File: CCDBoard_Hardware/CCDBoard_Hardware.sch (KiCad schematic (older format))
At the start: 3 parts

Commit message: Associated footprints and generated netlist
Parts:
- Conn1: renamed from Conn?; value Molex_SL_02 -> Molex_SL_04; footprint (none) -> MRDT_Connectors:MOLEX_SL_04_Horizontal
- Conn2: renamed from Conn?; footprint (none) -> MRDT_Connectors:MOLEX_SL_07_Horizontal
- U1: renamed from U?; footprint (none) -> MRDT_Sensors:TCD-1304
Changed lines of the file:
@@
 EESchema Schematic File Version 4
+LIBS:CCDBoard_Hardware-cache
 EELAYER 26 0
 EELAYER END
@@
 $EndDescr
 $Comp
-L MRDT_Sensors:TCD1304 U?
+L MRDT_Sensors:TCD1304 U1
 U 1 1 5C83DD52
 P 4500 2600
-F 0 "U?" H 4700 3175 50  0000 C CNN
+F 0 "U1" H 4700 3175 50  0000 C CNN
 F 1 "TCD1304" H 4700 3084 50  0000 C CNN
-F 2 "" H 4200 2100 50  0001 C CNN
+F 2 "MRDT_Sensors:TCD-1304" H 4200 2100 50  0001 C CNN
 F 3 "" H 4200 2100 50  0001 C CNN
 	1    4500 2600
@@
 $EndComp
 $Comp
-L power:GND #PWR?
+L power:GND #PWR0101
 U 1 1 5C83DDBD
 P 4350 2550
-F 0 "#PWR?" H 4350 2300 50  0001 C CNN
+F 0 "#PWR0101" H 4350 2300 50  0001 C CNN
 F 1 "GND" H 4355 2377 50  0000 C CNN
 F 2 "" H 4350 2550 50  0001 C CNN
@@
 $EndComp
 $Comp
-L power:+3V3 #PWR?
+L power:+3V3 #PWR0102
 U 1 1 5C83DE2E
 P 4350 2250
-F 0 "#PWR?" H 4350 2100 50  0001 C CNN
+F 0 "#PWR0102" H 4350 2100 50  0001 C CNN
 F 1 "+3V3" H 4365 2423 50  0000 C CNN
 F 2 "" H 4350 2250 50  0001 C CNN
@@
 	5050 2550 5000 2550
 $Comp
-L MRDT_Connectors:Molex_SL_07 Conn?
+L MRDT_Connectors:Molex_SL_07 Conn2
 U 1 1 5C83E06D
 P 6050 3800
-F 0 "Conn?" H 6050 3750 60  0000 L CNN
+F 0 "Conn2" H 6050 3750 60  0000 L CNN
 F 1 "Molex_SL_07" H 6177 4102 60  0000 L CNN
-F 2 "" H 6050 4000 60  0001 C CNN
+F 2 "MRDT_Connectors:MOLEX_SL_07_Horizontal" H 6050 4000 60  0001 C CNN
 F 3 "" H 6050 4000 60  0001 C CNN
 	1    6050 3800
@@
 $EndComp
 $Comp
-L power:+3V3 #PWR?
+L power:+3V3 #PWR0103
 U 1 1 5C83E099
 P 5800 3100
-F 0 "#PWR?" H 5800 2950 50  0001 C CNN
+F 0 "#PWR0103" H 5800 2950 50  0001 C CNN
 F 1 "+3V3" H 5815 3273 50  0000 C CNN
 F 2 "" H 5800 3100 50  0001 C CNN
@@
 $EndComp
 $Comp
-L power:GND #PWR?
+L power:GND #PWR0104
 U 1 1 5C83E0A8
 P 5800 3800
-F 0 "#PWR?" H 5800 3550 50  0001 C CNN
+F 0 "#PWR0104" H 5800 3550 50  0001 C CNN
 F 1 "GND" H 5805 3627 50  0000 C CNN
 F 2 "" H 5800 3800 50  0001 C CNN
@@
 $EndComp
 $Comp
-L MRDT_Connectors:Molex_SL_04 Conn?
+L MRDT_Connectors:Molex_SL_04 Conn1
 U 1 1 5C83E20B
 P 6050 2600
-F 0 "Conn?" H 6050 2550 60  0000 L CNN
-F 1 "Molex_SL_02" H 6177 2752 60  0000 L CNN
-F 2 "" H 6050 2500 60  0001 C CNN
+F 0 "Conn1" H 6050 2550 60  0000 L CNN
+F 1 "Molex_SL_04" H 6177 2752 60  0000 L CNN
+F 2 "MRDT_Connectors:MOLEX_SL_04_Horizontal" H 6050 2500 60  0001 C CNN
 F 3 "" H 6050 2500 60  0001 C CNN
 	1    6050 2600
@@
 $EndComp
 $Comp
-L power:GND #PWR?
+L power:GND #PWR0105
 U 1 1 5C83E23F
 P 5800 2600
-F 0 "#PWR?" H 5800 2350 50  0001 C CNN
+F 0 "#PWR0105" H 5800 2350 50  0001 C CNN
 F 1 "GND" H 5805 2427 50  0000 C CNN
 F 2 "" H 5800 2600 50  0001 C CNN

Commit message: updates Sensorboard connector
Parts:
- Conn1: value Molex_SL_04 -> Molex_SL_05; footprint MRDT_Connectors:MOLEX_SL_04_Horizontal -> MRDT_Connectors:MOLEX_SL_05_Horizontal; symbol MRDT_Connectors:Molex_SL_04 -> MRDT_Connectors:Molex_SL_05
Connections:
- wire segments 24 -> 26
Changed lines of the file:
@@
 $EndComp
 $Comp
-L MRDT_Connectors:Molex_SL_04 Conn1
+L MRDT_Connectors:Molex_SL_05 Conn1
 U 1 1 5C83E20B
 P 6050 2600
 F 0 "Conn1" H 6050 2550 60  0000 L CNN
-F 1 "Molex_SL_04" H 6177 2752 60  0000 L CNN
-F 2 "MRDT_Connectors:MOLEX_SL_04_Horizontal" H 6050 2500 60  0001 C CNN
+F 1 "Molex_SL_05" H 6177 2752 60  0000 L CNN
+F 2 "MRDT_Connectors:MOLEX_SL_05_Horizontal" H 6050 2500 60  0001 C CNN
 F 3 "" H 6050 2500 60  0001 C CNN
 	1    6050 2600
@@
 Text Notes 6650 2300 2    50   ~ 0
 Reading TIVA
+$Comp
+L power:+3V3 #PWR?
+U 1 1 5C84E599
+P 5800 2100
+F 0 "#PWR?" H 5800 1950 50  0001 C CNN
+F 1 "+3V3" H 5815 2273 50  0000 C CNN
+F 2 "" H 5800 2100 50  0001 C CNN
+F 3 "" H 5800 2100 50  0001 C CNN
+	1    5800 2100
+	1    0    0    -1
+$EndComp
+Wire Wire Line
+	5850 2150 5800 2150
+Wire Wire Line
+	5800 2150 5800 2100
 $EndSCHEMATC

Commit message: Layout and step
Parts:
- Conn1: footprint MRDT_Connectors:MOLEX_SL_05_Horizontal -> MRDT_Connectors:MOLEX_SL_05_Vertical
- Conn2: footprint MRDT_Connectors:MOLEX_SL_07_Horizontal -> MRDT_Connectors:MOLEX_SL_07_Vertical
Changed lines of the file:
@@
 F 0 "Conn2" H 6050 3750 60  0000 L CNN
 F 1 "Molex_SL_07" H 6177 4102 60  0000 L CNN
-F 2 "MRDT_Connectors:MOLEX_SL_07_Horizontal" H 6050 4000 60  0001 C CNN
+F 2 "MRDT_Connectors:MOLEX_SL_07_Vertical" H 6050 4000 60  0001 C CNN
 F 3 "" H 6050 4000 60  0001 C CNN
 	1    6050 3800
@@
 F 0 "Conn1" H 6050 2550 60  0000 L CNN
 F 1 "Molex_SL_05" H 6177 2752 60  0000 L CNN
-F 2 "MRDT_Connectors:MOLEX_SL_05_Horizontal" H 6050 2500 60  0001 C CNN
+F 2 "MRDT_Connectors:MOLEX_SL_05_Vertical" H 6050 2500 60  0001 C CNN
 F 3 "" H 6050 2500 60  0001 C CNN
 	1    6050 2600
@@
 Reading TIVA
 $Comp
-L power:+3V3 #PWR?
+L power:+3V3 #PWR0106
 U 1 1 5C84E599
 P 5800 2100
-F 0 "#PWR?" H 5800 1950 50  0001 C CNN
+F 0 "#PWR0106" H 5800 1950 50  0001 C CNN
 F 1 "+3V3" H 5815 2273 50  0000 C CNN
 F 2 "" H 5800 2100 50  0001 C CNN

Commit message: Making new symbols and board for spec
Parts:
- removed Conn1: Molex_SL_05, MRDT_Connectors:MOLEX_SL_05_Vertical, symbol MRDT_Connectors:Molex_SL_05
- removed Conn2: Molex_SL_07, MRDT_Connectors:MOLEX_SL_07_Vertical, symbol MRDT_Connectors:Molex_SL_07
- removed U1: TCD1304, MRDT_Sensors:TCD-1304, symbol MRDT_Sensors:TCD1304
- added U?: S11639-01, symbol MRDT_ICs:S11639-01
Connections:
- net labels removed: +3V3, GND, ICG, M, OS, SH, Sync1, Sync2
- wire segments 26 -> 0
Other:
- note removed: "Clocking TIVA"
- note removed: "Reading TIVA"
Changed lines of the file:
@@
 EESchema Schematic File Version 4
 LIBS:CCDBoard_Hardware-cache
-EELAYER 26 0
+EELAYER 30 0
 EELAYER END
 $Descr A4 11693 8268
@@
 $EndDescr
 $Comp
-L MRDT_Sensors:TCD1304 U1
-U 1 1 5C83DD52
-P 4500 2600
-F 0 "U1" H 4700 3175 50  0000 C CNN
-F 1 "TCD1304" H 4700 3084 50  0000 C CNN
-F 2 "MRDT_Sensors:TCD-1304" H 4200 2100 50  0001 C CNN
-F 3 "" H 4200 2100 50  0001 C CNN
-	1    4500 2600
+L MRDT_ICs:S11639-01 U?
+U 1 1 5D9443A9
+P 2100 1200
+F 0 "U?" H 2100 1325 50  0000 C CNN
+F 1 "S11639-01" H 2100 1234 50  0000 C CNN
+F 2 "" H 2100 1200 50  0001 C CNN
+F 3 "" H 2100 1200 50  0001 C CNN
+	1    2100 1200
 	1    0    0    -1
 $EndComp
-$Comp
-L power:GND #PWR0101
-U 1 1 5C83DDBD
-P 4350 2550
-F 0 "#PWR0101" H 4350 2300 50  0001 C CNN
-F 1 "GND" H 4355 2377 50  0000 C CNN
-F 2 "" H 4350 2550 50  0001 C CNN
-F 3 "" H 4350 2550 50  0001 C CNN
-	1    4350 2550
-	1    0    0    -1
-$EndComp
-$Comp
-L power:+3V3 #PWR0102
-U 1 1 5C83DE2E
-P 4350 2250
-F 0 "#PWR0102" H 4350 2100 50  0001 C CNN
-F 1 "+3V3" H 4365 2423 50  0000 C CNN
-F 2 "" H 4350 2250 50  0001 C CNN
-F 3 "" H 4350 2250 50  0001 C CNN
-	1    4350 2250
-	1    0    0    -1
-$EndComp
-Wire Wire Line
-	4400 2500 4350 2500
-Wire Wire Line
-	4350 2500 4350 2550
-Wire Wire Line
-	4400 2400 4350 2400
-Wire Wire Line
-	4350 2400 4350 2300
-Wire Wire Line
-	4400 2300 4350 2300
-Connection ~ 4350 2300
-Wire Wire Line
-	4350 2300 4350 2250
-Text GLabel 5800 3650 0    50   Output ~ 0
-M
-Text GLabel 5800 3550 0    50   Output ~ 0
-SH
-Text GLabel 5800 3450 0    50   Output ~ 0
-ICG
-Text GLabel 5800 2450 0    50   Input ~ 0
-OS
-Wire Wire Line
-	5000 2250 5050 2250
-Wire Wire Line
-	5000 2350 5050 2350
-Wire Wire Line
-	5000 2450 5050 2450
-Wire Wire Line
-	5050 2550 5000 2550
-$Comp
-L MRDT_Connectors:Molex_SL_07 Conn2
-U 1 1 5C83E06D
-P 6050 3800
-F 0 "Conn2" H 6050 3750 60  0000 L CNN
-F 1 "Molex_SL_07" H 6177 4102 60  0000 L CNN
-F 2 "MRDT_Connectors:MOLEX_SL_07_Vertical" H 6050 4000 60  0001 C CNN
-F 3 "" H 6050 4000 60  0001 C CNN
-	1    6050 3800
-	1    0    0    -1
-$EndComp
-$Comp
-L power:+3V3 #PWR0103
-U 1 1 5C83E099
-P 5800 3100
-F 0 "#PWR0103" H 5800 2950 50  0001 C CNN
-F 1 "+3V3" H 5815 3273 50  0000 C CNN
-F 2 "" H 5800 3100 50  0001 C CNN
-F 3 "" H 5800 3100 50  0001 C CNN
-	1    5800 3100
-	1    0    0    -1
-$EndComp
-$Comp
-L power:GND #PWR0104
-U 1 1 5C83E0A8
-P 5800 3800
-F 0 "#PWR0104" H 5800 3550 50  0001 C CNN
-F 1 "GND" H 5805 3627 50  0000 C CNN
-F 2 "" H 5800 3800 50  0001 C CNN
-F 3 "" H 5800 3800 50  0001 C CNN
-	1    5800 3800
-	1    0    0    -1
-$EndComp
-$Comp
-L MRDT_Connectors:Molex_SL_05 Conn1
-U 1 1 5C83E20B
-P 6050 2600
-F 0 "Conn1" H 6050 2550 60  0000 L CNN
-F 1 "Molex_SL_05" H 6177 2752 60  0000 L CNN
-F 2 "MRDT_Connectors:MOLEX_SL_05_Vertical" H 6050 2500 60  0001 C CNN
-F 3 "" H 6050 2500 60  0001 C CNN
-	1    6050 2600
-	1    0    0    -1
-$EndComp
-$Comp
-L power:GND #PWR0105
-U 1 1 5C83E23F
-P 5800 2600
-F 0 "#PWR0105" H 5800 2350 50  0001 C CNN
-F 1 "GND" H 5805 2427 50  0000 C CNN
-F 2 "" H 5800 2600 50  0001 C CNN
-F 3 "" H 5800 2600 50  0001 C CNN
-	1    5800 2600
-	1    0    0    -1
-$EndComp
-Text GLabel 5050 2250 2    50   Input ~ 0
-M
-Text GLabel 5050 2350 2    50   Input ~ 0
-SH
-Text GLabel 5050 2450 2    50   Input ~ 0
-ICG
-Text GLabel 5050 2550 2    50   Output ~ 0
-OS
-Wire Wire Line
-	5850 3450 5800 3450
-Wire Wire Line
-	5850 3550 5800 3550
-Wire Wire Line
-	5850 3650 5800 3650
-Wire Wire Line
-	5850 3750 5800 3750
-Wire Wire Line
-	5800 3750 5800 3800
-Wire Wire Line
-	5850 3150 5800 3150
-Wire Wire Line
-	5800 3150 5800 3100
-Text GLabel 5800 3350 0    50   Output ~ 0
-Sync1
-Text GLabel 5800 3250 0    50   Output ~ 0
-Sync2
-Wire Wire Line
-	5850 3250 5800 3250
-Wire Wire Line
-	5850 3350 5800 3350
-Text GLabel 5800 2350 0    50   Input ~ 0
-Sync1
-Text GLabel 5800 2250 0    50   Input ~ 0
-Sync2
-Wire Wire Line
-	5850 2550 5800 2550
-Wire Wire Line
-	5800 2550 5800 2600
-Wire Wire Line
-	5850 2450 5800 2450
-Wire Wire Line
-	5850 2350 5800 2350
-Wire Wire Line
-	5850 2250 5800 2250
-Text Notes 6700 3200 2    50   ~ 0
-Clocking TIVA
-Text Notes 6650 2300 2    50   ~ 0
-Reading TIVA
-$Comp
-L power:+3V3 #PWR0106
-U 1 1 5C84E599
-P 5800 2100
-F 0 "#PWR0106" H 5800 1950 50  0001 C CNN
-F 1 "+3V3" H 5815 2273 50  0000 C CNN
-F 2 "" H 5800 2100 50  0001 C CNN
-F 3 "" H 5800 2100 50  0001 C CNN
-	1    5800 2100
-	1    0    0    -1
-$EndComp
-Wire Wire Line
-	5850 2150 5800 2150
-Wire Wire Line
-	5800 2150 5800 2100
 $EndSCHEMATC

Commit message: New shematic
this might be completly wrong. IDK
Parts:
- added C? (x6): C_Small, symbol Device:C_Small
- added C? (x4): CP_Small, symbol Device:CP_Small
- added R? (x4): R, symbol Device:R
- added U?: OPAMP, symbol pspice:OPAMP
- U?: symbol MRDT_ICs:S11639-01 -> CCDBoard_Hardware-rescue:S11639-01-MRDT_ICs
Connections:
- net labels added: +5V, 0, Video
- wire segments 0 -> 67

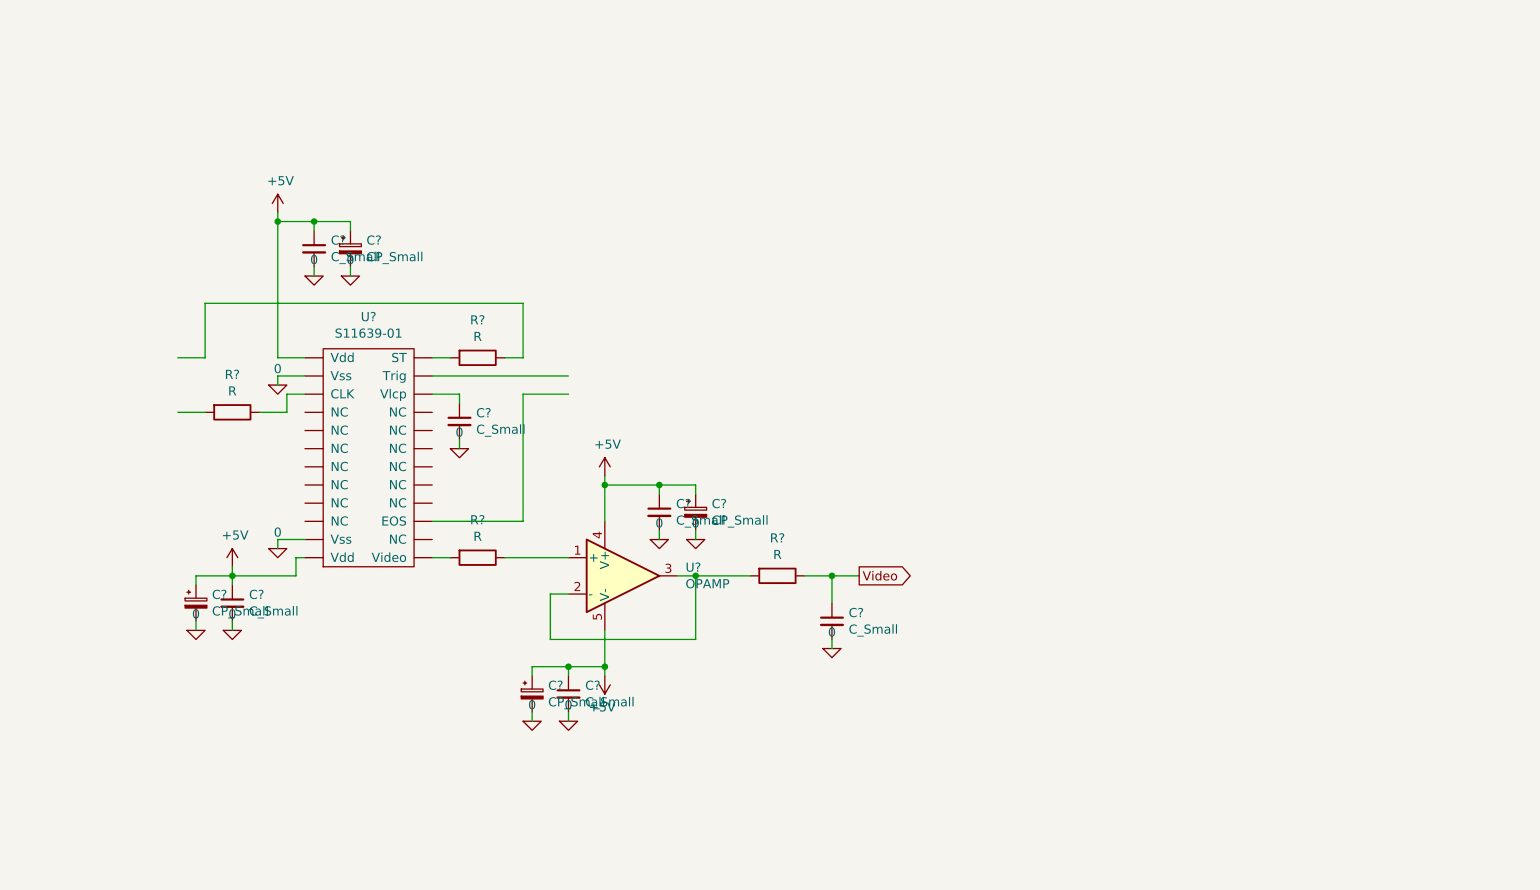
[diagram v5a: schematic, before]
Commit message: Redoing schematic for neatness
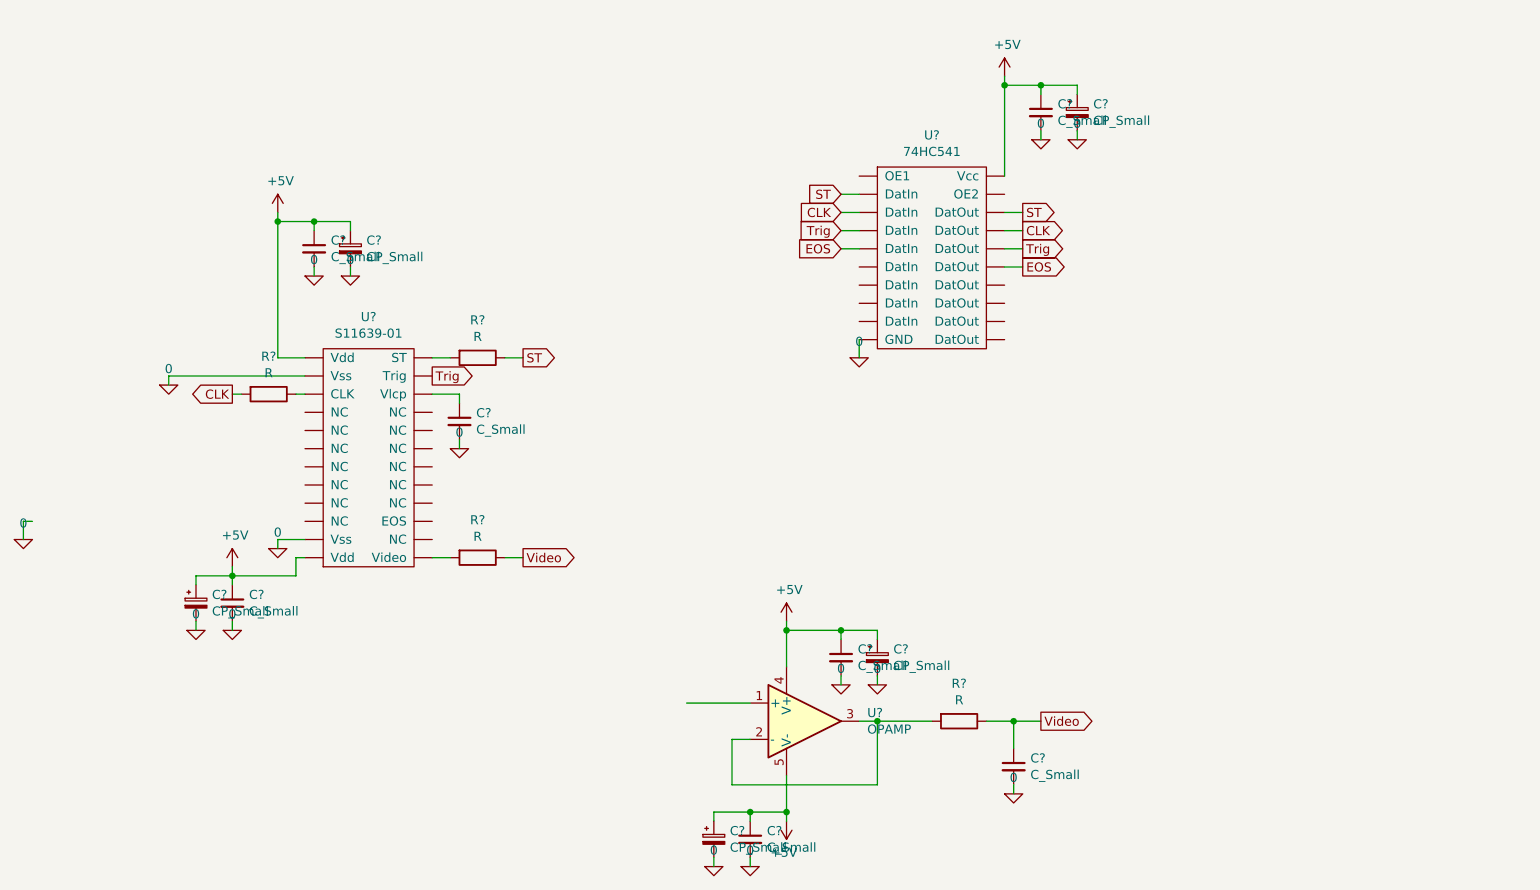
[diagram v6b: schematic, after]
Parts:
- added C?: C_Small, symbol Device:C_Small
- added C?: CP_Small, symbol Device:CP_Small
- added U?: 74HC541, symbol MRDT_ICs:74HC541
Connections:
- net labels added: CLK, EOS, ST, Trig
- wire segments 67 -> 77
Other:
- moved on the sheet: C?, R?, U?

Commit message: Revision made. Much cleaner
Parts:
- removed C? (x3): C_Small, symbol Device:C_Small
- removed C? (x2): CP_Small, symbol Device:CP_Small
- removed R?: R, symbol Device:R
- removed U?: OPAMP, symbol pspice:OPAMP
- added C? (x3): C_Small, symbol Device:C_Small
- added C? (x2): CP_Small, symbol Device:CP_Small
- added R?: R, symbol Device:R
- added U?: LT1818, symbol MRDT_ICs:LT1818
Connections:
- net +5V: now also C?.1, C?.1, C?.1, C?.1, U?.~ (V-)
- net 0: now also C?.2, C?.2, C?.2, C?.2, C?.2
- net Video: now also C?.1, R?.2, U?.~ (V-)
- new net -IN: R?.1, U?.~ (V-)
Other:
- moved on the sheet: C?, U?
